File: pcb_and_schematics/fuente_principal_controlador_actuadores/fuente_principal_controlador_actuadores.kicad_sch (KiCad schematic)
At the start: 17 parts

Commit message: revisión del circuito de pcb
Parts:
- T1: renamed from T?; value Transformer_1P_1S -> Transformer 12V 10A
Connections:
- net 3.3V ec: no longer J?.1 (VBUS)
- net signal EC: now also J?.1 (VBUS)
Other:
- moved on the sheet: C1, C2, C3, D?, F1, J?, R, R?, T1, U?

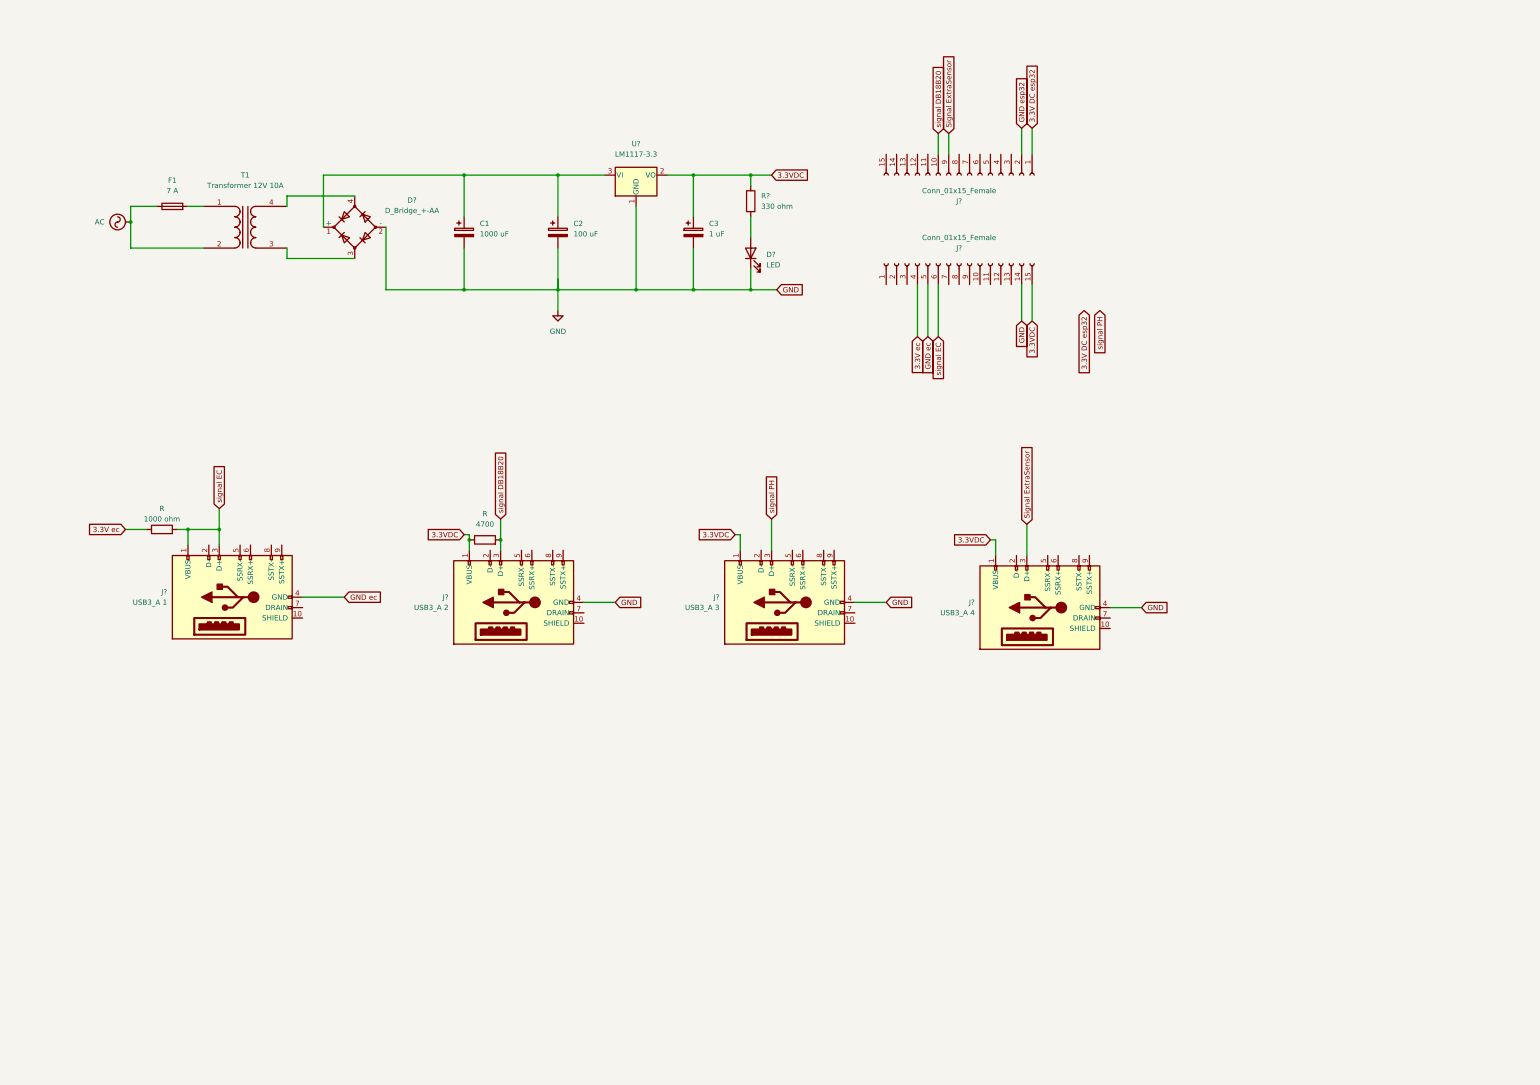
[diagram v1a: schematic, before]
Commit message: otros adelantos en el diseño de la pcb
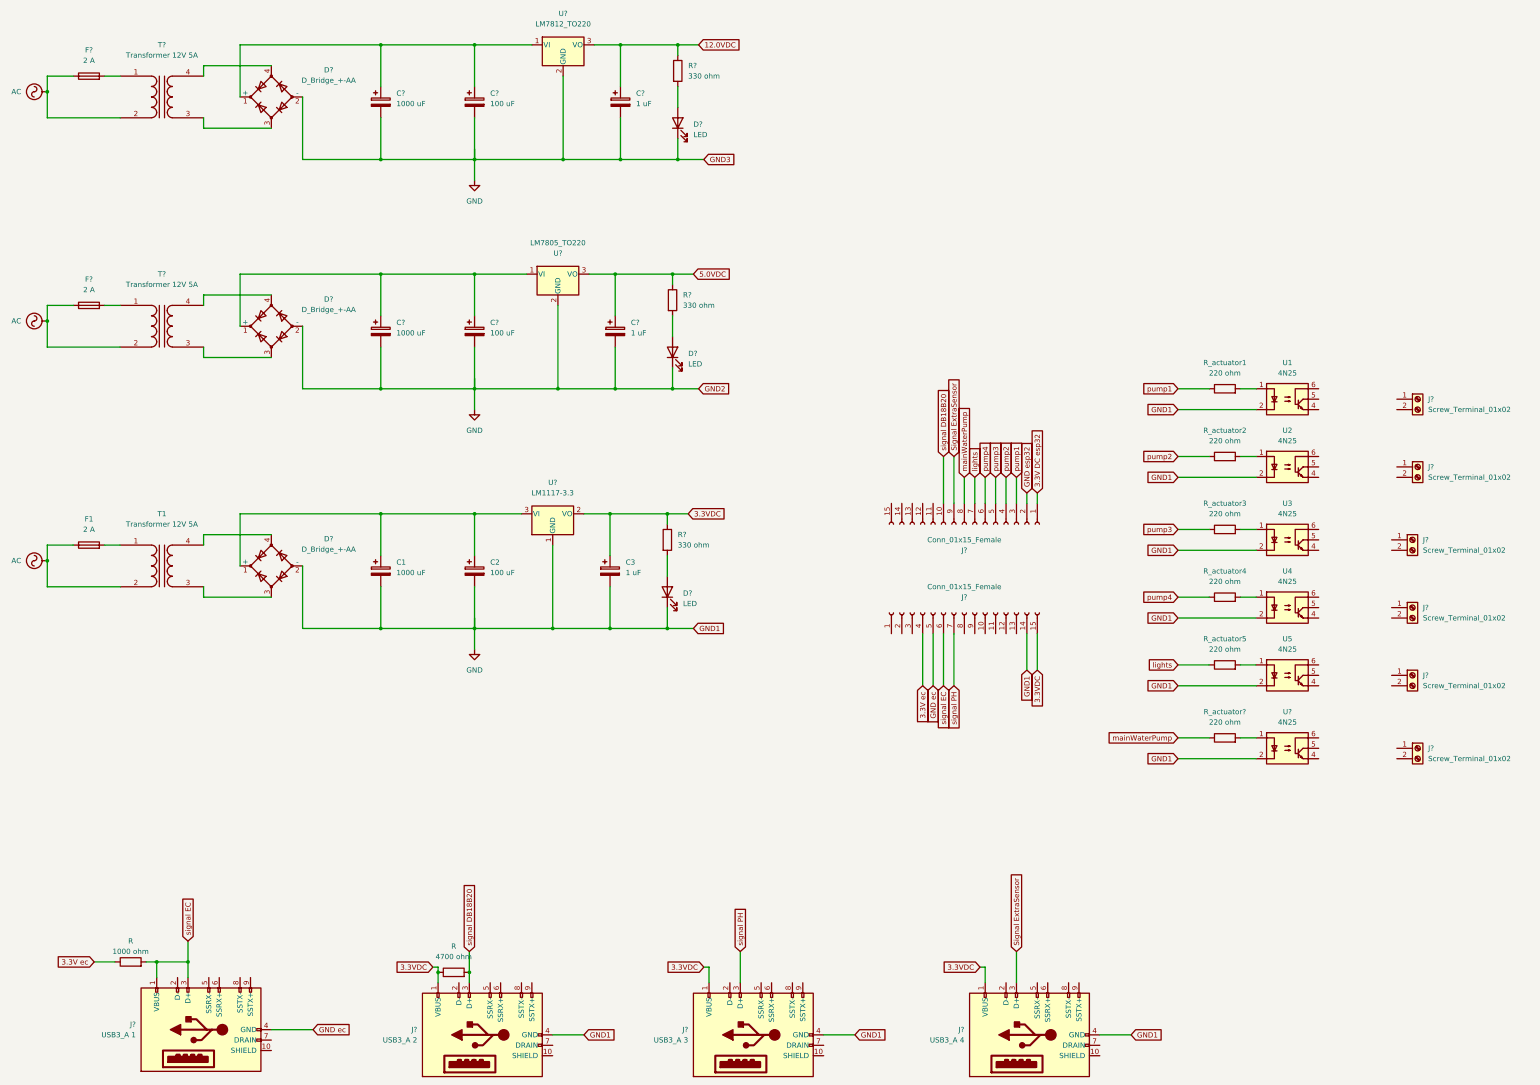
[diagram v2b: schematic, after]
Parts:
- added C? (x2): 100 uF, symbol Device:C_Polarized
- added C? (x2): 1 uF, symbol Device:C_Polarized
- added C? (x2): 1000 uF, symbol Device:C_Polarized
- added D? (x2): LED, symbol Device:LED
- added D? (x2): D_Bridge_+-AA, symbol Device:D_Bridge_+-AA
- added F? (x2): 2 A, symbol Device:Fuse
- added J? (x6): Screw_Terminal_01x02, symbol Connector:Screw_Terminal_01x02
- added R? (x2): 330 ohm, symbol Device:R
- added R_actuator1, R_actuator2, R_actuator3, R_actuator4, R_actuator5, R_actuator?: 220 ohm, symbol Device:R
- added T? (x2): Transformer 12V 5A, symbol Device:Transformer_1P_1S
- added U1, U2, U3, U4, U5, U?: 4N25, Package_DIP:DIP-6_W7.62mm, symbol Isolator:4N25
- added U?: LM7812_TO220, Package_TO_SOT_THT:TO-220-3_Vertical, symbol Regulator_Linear:LM7812_TO220
- added U?: LM7805_TO220, Package_TO_SOT_THT:TO-220-3_Vertical, symbol Regulator_Linear:LM7805_TO220
- F1: value 7 A -> 2 A
- R: value 4700 -> 4700 ohm
- T1: value Transformer 12V 10A -> Transformer 12V 5A
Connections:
- net AC: now also F?.1, F?.1, T?.2 (AB), T?.2 (AB)
- net GND: now also C?.2, C?.2, C?.2, C?.2, C?.2, C?.2, D?.1 (K), D?.1 (K), D?.2 (-), D?.2 (-), U1.2, U2.2, U3.2, U4.2, U5.2, U?.2, U?.2 (GND), U?.2 (GND)
- net signal PH: now also J?.7 (Pin_7)
- net pump1: now reaches J?.3 (Pin_3)
- net pump1: now also R_actuator1.1
- net pump2: now reaches J?.4 (Pin_4)
- net pump2: now also R_actuator2.1
- net pump3: now reaches J?.5 (Pin_5)
- net pump3: now also R_actuator3.1
- net pump4: now reaches J?.6 (Pin_6)
- net pump4: now also R_actuator4.1
- net lights: now reaches J?.7 (Pin_7)
- net lights: now also R_actuator5.1
- net mainWaterPump: now reaches J?.8 (Pin_8)
- net mainWaterPump: now also R_actuator?.1
- new net: R_actuator3.2, U3.1
- new net: F?.2, T?.1 (AA) (x2)
- new net: D?.2 (A), R?.2 (x2)
- new net: R_actuator1.2, U1.1
- new net: C?.1, C?.1, D?.1 (+), U?.1 (VI) (x2)
- new net: R_actuator4.2, U4.1
- new net: R_actuator2.2, U2.1
- new net: D?.3, T?.3 (SA) (x2)
- new net: D?.4, T?.4 (SB) (x2)
- new net: R_actuator?.2, U?.1
- new net: R_actuator5.2, U5.1
- new net 12.0VDC: C?.1, R?.1, U?.3 (VO)
- new net 5.0VDC: C?.1, R?.1, U?.3 (VO)
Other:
- moved on the sheet: C1, C2, C3, D?, F1, J?, R, R?, T1, U?

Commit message: minimal change to pcb layout
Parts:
- removed C?: 100 uF, symbol Device:C_Polarized
- removed C?: 1000 uF, symbol Device:C_Polarized
- removed D?: D_Bridge_+-AA, symbol Device:D_Bridge_+-AA
- removed F?: 2 A, symbol Device:Fuse
- removed T?: Transformer 12V 5A, symbol Device:Transformer_1P_1S
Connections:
- net at U?.1 (VI): now also C?.1, C?.1, D?.1 (+), U?.1 (VI)
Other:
- moved on the sheet: C?, D?, F?, T?

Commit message: eliminado de fuente de alimentación en el circuito, debido a que se va a comprar una ya hecha
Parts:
- removed C?: 100 uF, symbol Device:C_Polarized
- removed C?: 1000 uF, symbol Device:C_Polarized
- removed D? (x2): D_Bridge_+-AA, symbol Device:D_Bridge_+-AA
- removed F1, F?: 2 A, symbol Device:Fuse
- removed T1, T?: Transformer 12V 5A, symbol Device:Transformer_1P_1S
- added C?: 100 uF, symbol Device:C_Polarized
- added C?: 1000 uF, symbol Device:C_Polarized
- added J? (x4): Screw_Terminal_01x02, symbol Connector:Screw_Terminal_01x02
- added R_actuator? (x2): 220 ohm, symbol Device:R
- added U7, U?: 4N25, Package_DIP:DIP-6_W7.62mm, symbol Isolator:4N25
- gave numbers to parts that had none: 1
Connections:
- net extraActuator5V: now reaches J?.14 (Pin_14)
- net extraActuator5V: now also R_actuator?.1
- net extraActuator12V: now reaches J?.15 (Pin_15)
- net extraActuator12V: now also R_actuator?.1
- net at C1.1, C2.1, U?.3 (VI): now also J?.2 (Pin_2)
- net at U?.1 (VI), U?.1 (VI): now also C?.1, C?.1, J?.2 (Pin_2)
- net GND renamed GND 3.3V
- net GND 3.3V: now also J?.1 (Pin_1), U7.2, U?.2; no longer C?.2, C?.2, D?.1 (K), D?.1 (K), U?.2 (GND), U?.2 (GND)
- new net: R_actuator?.2, U7.1
- new net: R_actuator?.2, U?.1
- new net GND 12.0V: C?.2, C?.2, C?.2, C?.2, D?.1 (K), D?.1 (K), J?.1 (Pin_1), U?.2 (GND), U?.2 (GND)
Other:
- moved on the sheet: C1, C2, C3, C?, D?, J?, R, R?, R_actuator1, R_actuator2, R_actuator3, R_actuator4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

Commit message: mejoras en el circuito de control
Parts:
- removed J? (x7): Screw_Terminal_01x02, symbol Connector:Screw_Terminal_01x02
- added D? (x8): LED, symbol Device:LED
- added J?: Screw_Terminal_01x02, symbol Connector:Screw_Terminal_01x02
- added Q? (x2): TIP122, Package_TO_SOT_THT:TO-220-3_Vertical, symbol Transistor_BJT:TIP122
- added R? (x4): R, symbol Device:R
- added R? (x2): 10k ohm, symbol Device:R
- added U? (x2): 40106, symbol 4xxx:40106
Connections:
- net 5.0VDC: now also R?.2, R?.2, R?.2, R?.2
- net GND 12.0V: now also J?.2 (Pin_2), U7.4, U?.4, J?.2 (Pin_2)
- net GND 3.3V: now also D?.1 (K), D?.1 (K), D?.1 (K), D?.1 (K), D?.1 (K), D?.1 (K), D?.1 (K), D?.1 (K)
- net at R_actuator3.2, U3.1: now also D?.2 (A)
- net at R_actuator1.2, U1.1: now also D?.2 (A)
- net at R_actuator4.2, U4.1: now also D?.2 (A)
- net at R_actuator2.2, U2.1: now also D?.2 (A)
- net at R_actuator?.2, U6.1: now also D?.2 (A)
- net at R_actuator5.2, U5.1: now also D?.2 (A)
- net at R_actuator?.2, U7.1: now also D?.2 (A)
- net at U7.5: now also R?.1, U?.1
- net at R_actuator?.2, U?.1: now also D?.2 (A)
- net at J?.1 (Pin_1): now also Q?.3 (E)
- net at U?.5: now also R?.1, U?.1
- new net: Q?.1 (B), R?.2 (x2)
- new net: Q?.2 (C), R?.1 (x2)
- new net: J?.1 (Pin_1), Q?.3 (E)
- new net: R?.1, U?.2 (x2)
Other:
- moved on the sheet: J?, R_actuator1, R_actuator2, R_actuator3, R_actuator4, R_actuator5, R_actuator?, U1, U2, U3, U4, U5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

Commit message: avances en diseño de la pcb, de control y medicion de ph, ec y temperatura del agua
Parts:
- removed D? (x8): LED, symbol Device:LED
- removed R? (x2): R, symbol Device:R
- added J? (x6): Screw_Terminal_01x02, symbol Connector:Screw_Terminal_01x02
- added Q? (x6): TIP122, Package_TO_SOT_THT:TO-220-3_Vertical, symbol Transistor_BJT:TIP122
- added R? (x6): 10 ohm, symbol Device:R
- added R? (x6): 10k ohm, symbol Device:R
- added U? (x6): 40106, symbol 4xxx:40106
- R: renamed from R?; value R -> 10 ohm
- R?: value R -> 10 ohm
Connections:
- net 12.0VDC: now also Q?.2 (C), Q?.2 (C), Q?.2 (C)
- net 5.0VDC: now also Q?.2 (C), Q?.2 (C), Q?.2 (C), Q?.2 (C), Q?.2 (C), R?.2, R?.2, R?.2, R?.2, R?.2, R?.2
- net GND 12.0V: now also U1.4, U2.4, U3.4, U4.4, U5.4, U6.4, J?.2 (Pin_2), J?.2 (Pin_2), J?.2 (Pin_2), J?.2 (Pin_2), J?.2 (Pin_2), J?.2 (Pin_2)
- net at U3.5: now also R?.1, U?.9
- net at R.1: now also U?.4; no longer U?.2
- net at U6.5: now also R?.1, U?.1
- net at R?.1, U7.5: now also U?.3; no longer U?.1
- net at U1.5: now also R?.1, U?.13
- net at U5.5: now also R?.1, U?.3
- net at U4.5: now also R?.1, U?.5
- net at U2.5: now also R?.1, U?.11
- new net: J?.1 (Pin_1), Q?.3 (E) (x6)
- new net: R?.1, U?.8
- new net: Q?.1 (B), R?.2 (x6)
- new net: R?.1, U?.2
- new net: R?.1, U?.12
- new net: R?.1, U?.10
- new net: R?.1, U?.4
- new net: R?.1, U?.6
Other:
- moved on the sheet: J?, Q?, R, R_actuator1, R_actuator2, R_actuator3, R_actuator4, R_actuator5, R_actuator?, U1, U2, U3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

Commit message: avances en diseño de la pcb, de control y medicion de ph, ec y temperatura del agua
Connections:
- net 12.0VDC: now also R?.2, R?.2, R?.2
- net 3.3V DC esp32: now also U?.2; no longer J?.1 (Pin_1)
- net 5.0VDC: no longer R?.2, R?.2, R?.2
- net GND 3.3V: no longer U?.2
- net GND 12.0V renamed GND potencia
- net GND esp32: no longer names the net of J?.2 (Pin_2)

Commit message: adelantos en la creacion de la pcb a partir de los esquematicos
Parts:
- removed C2, C?: 100 uF, symbol Device:C_Polarized
- C1: renamed from C?; value 1000 uF -> 400 uF; footprint (none) -> maticas:electrolitic_capacitor_470uF
- C2, C3: renamed from C?; footprint (none) -> maticas:electrolitic_capacitor_470uF
- C4: renamed from C1; value 1000 uF -> 400 uF; footprint (none) -> maticas:electrolitic_capacitor_470uF
- C5: renamed from C3; footprint (none) -> maticas:electrolitic_capacitor_470uF
- D1, D2: renamed from D?; footprint (none) -> LED_THT:LED_D3.0mm
- R1, R2, R3: renamed from R?; footprint (none) -> Resistor_THT:R_Axial_DIN0204_L3.6mm_D1.6mm_P5.08mm_Horizontal
- gave numbers to parts that had none: 47
- renumbered U7 to Opto2, U6 to Opto3, U5 to Opto4, U4 to Opto5, U3 to Opto6, U2 to Opto7, U1 to Opto8, R_actuator5 to R_actuator4, R_actuator4 to R_actuator5, R_actuator3 to R_actuator6, R_actuator2 to R_actuator7, R_actuator1 to R_actuator9, R to Rsensor1, R to Rsensor2, R to Rtransistor2
